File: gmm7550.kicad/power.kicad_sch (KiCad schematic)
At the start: 48 parts, among them Q1 NX6008NBK, U11 TPS3840DL28DBV, U12 ADP2164, U13 ADP2164, U3 ADP1753

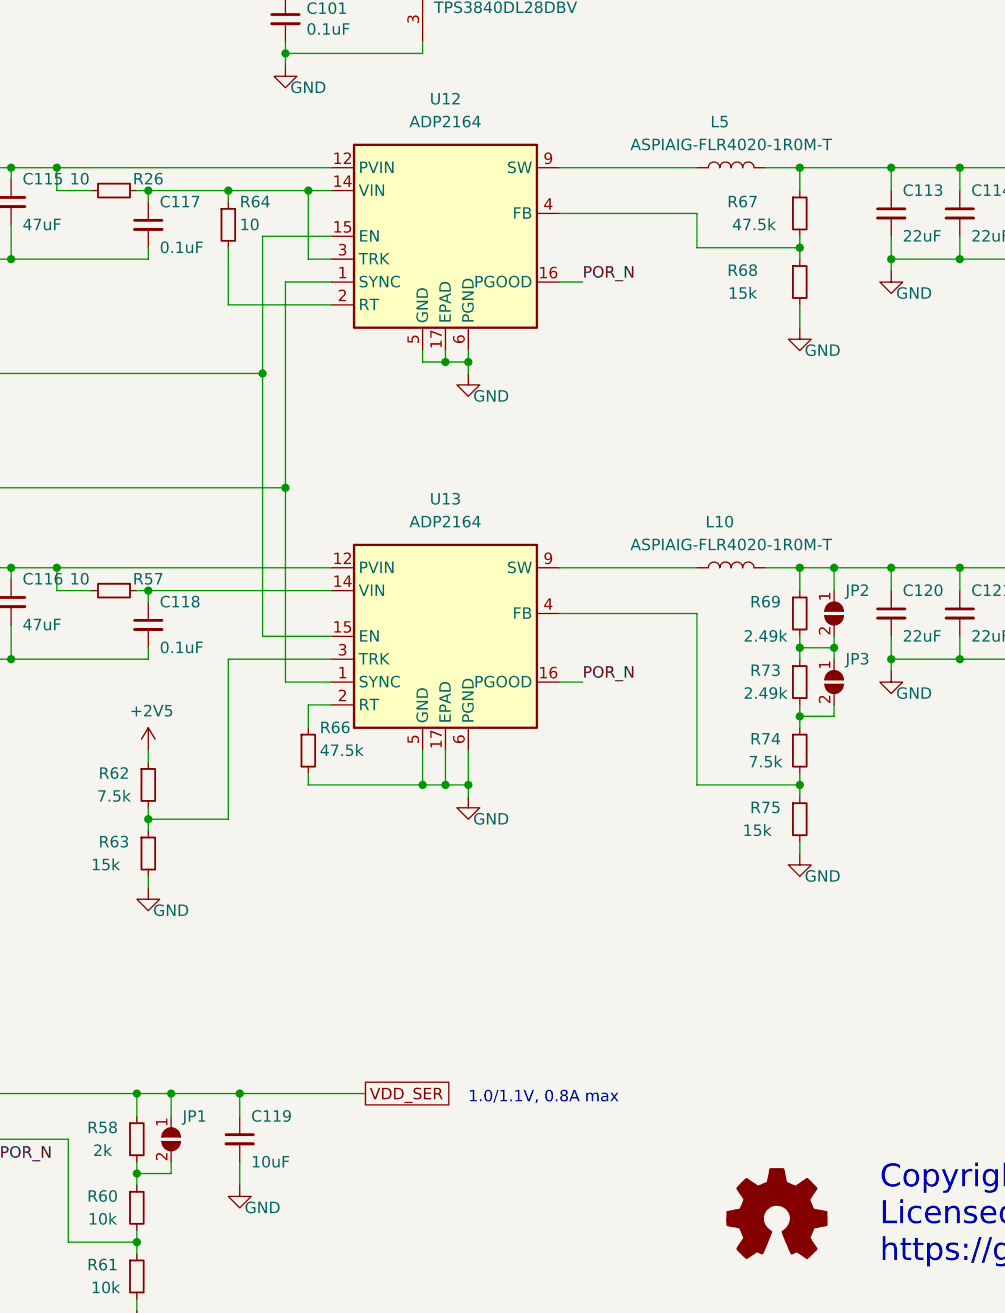
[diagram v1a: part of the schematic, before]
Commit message: Update designs to KiCad v7
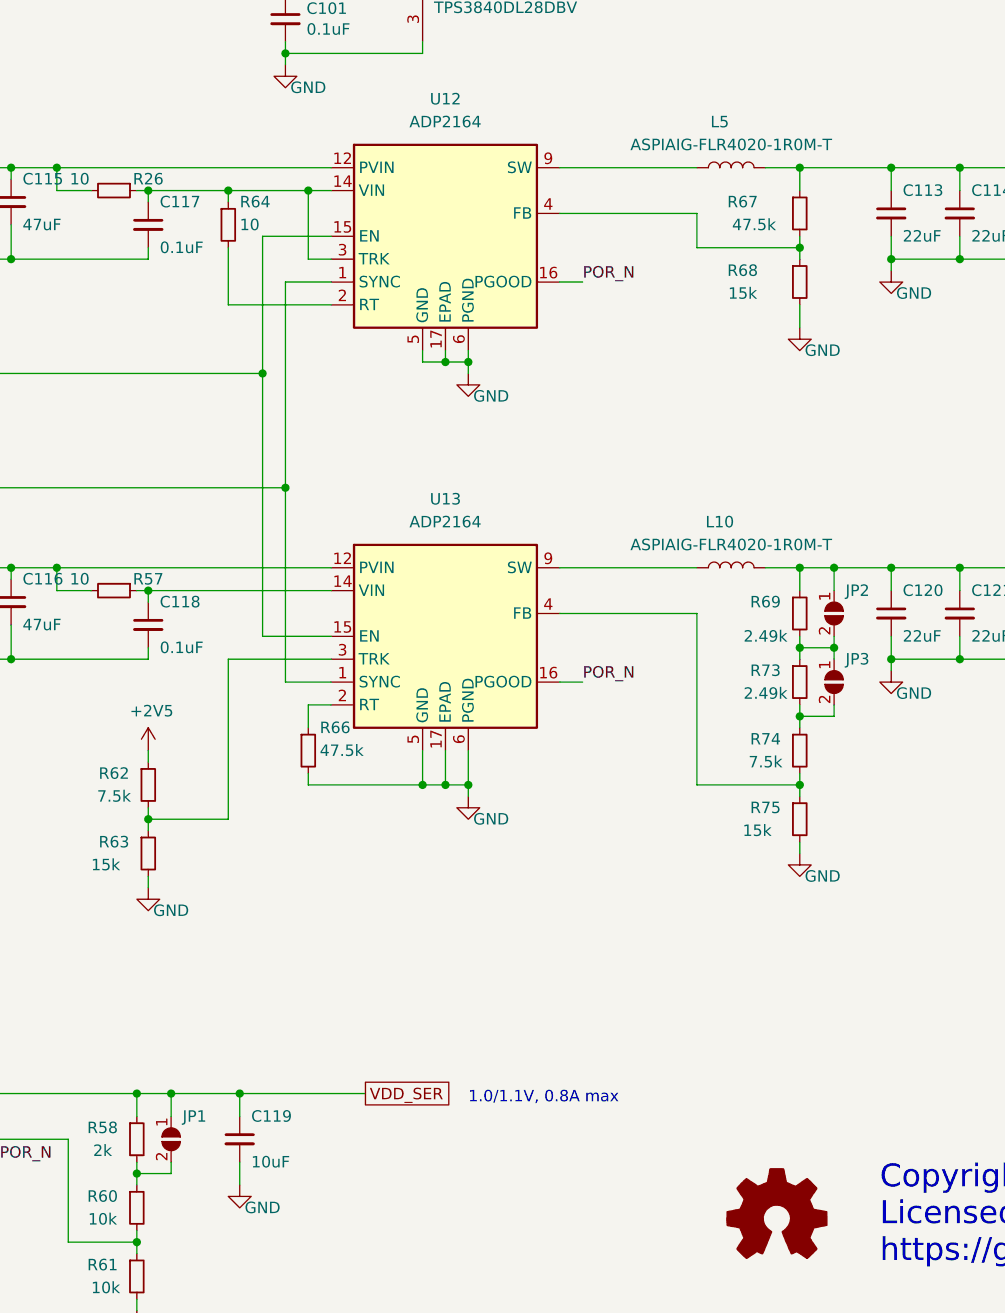
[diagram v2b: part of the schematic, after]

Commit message: Update copyright years and increment revision
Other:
- note added: "Copyright (c) 2020-2024 Anton Kuzmin Licensed under CERN-OHL-P v2 https://github.com/gmm-7550/"
- note removed: "Copyright (c) 2020-2022 Anton Kuzmin Licensed under CERN-OHL-P v2 https://github.com/ak-fau/gmm7550.git"
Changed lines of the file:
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@@
   (title_block
     (title "GateMate FPGA Module: GMM-7550")
-    (date "2022-04-24")
-    (rev "2.1")
+    (date "2022-04-27")
+    (rev "2.2")
   )
   (junction (at 129.54 80.01) (diameter 0) (color 0 0 0 0)
@@
     (effects (font (size 1.27 1.27)) (justify left bottom))
   )
-  (text "Copyright (c) 2020-2022  Anton Kuzmin\nLicensed under CERN-OHL-P v2\nhttps://github.com/ak-fau/gmm7550.git"
+  (text "Copyright (c) 2020-2024  Anton Kuzmin\nLicensed under CERN-OHL-P v2\nhttps://github.com/gmm-7550/"
     (at 198.12 179.07 0)
     (effects (font (size 2.54 2.54)) (justify left bottom))

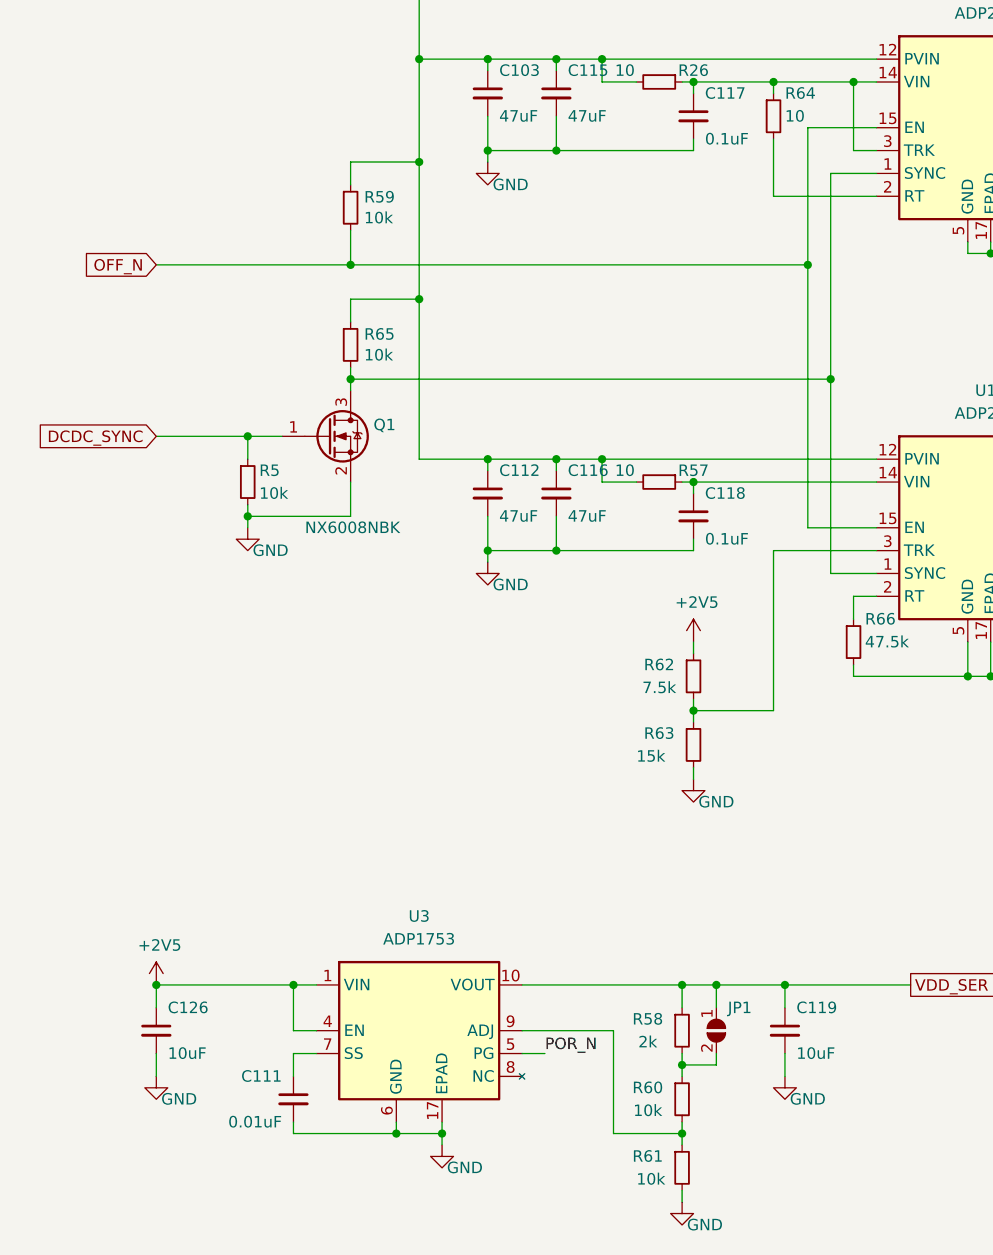
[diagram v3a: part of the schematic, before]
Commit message: Minor updates based on the test results
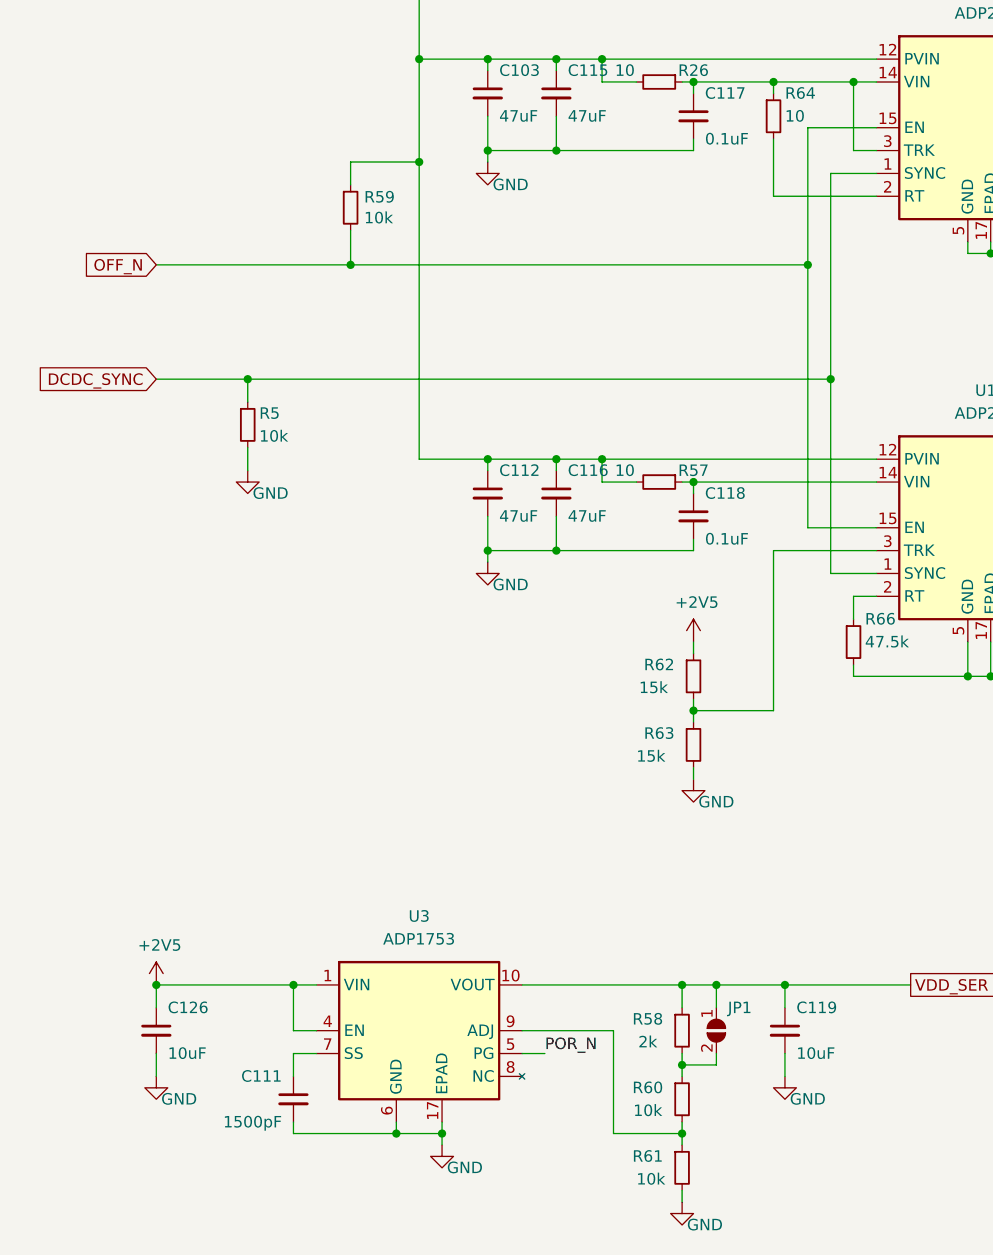
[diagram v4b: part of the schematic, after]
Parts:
- removed Q1: NX6008NBK, Package_TO_SOT_SMD:SOT-23, symbol Device:Q_NMOS_GSD
- removed R65: 10k, Resistor_SMD:R_0402_1005Metric, symbol Device:R_Small
- C111: value 0.01uF -> 1500pF
- R62: value 7.5k -> 15k
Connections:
- net DCDC_SYNC: now also U12.1 (SYNC), U13.1 (SYNC)
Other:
- moved on the sheet: R5
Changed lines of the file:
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@@
   (junction (at 93.98 111.76) (diameter 0) (color 0 0 0 0)
   )
-  (junction (at 67.31 99.06) (diameter 0) (color 0 0 0 0)
+  (junction (at 67.31 92.71) (diameter 0) (color 0 0 0 0)
   )
   (junction (at 214.63 67.31) (diameter 0) (color 0 0 0 0)
   )
-  (junction (at 67.31 107.95) (diameter 0) (color 0 0 0 0)
-  )
   (junction (at 78.74 80.01) (diameter 0) (color 0 0 0 0)
   )
@@
   (junction (at 207.01 67.31) (diameter 0) (color 0 0 0 0)
   )
-  (junction (at 78.74 92.71) (diameter 0) (color 0 0 0 0)
-  )
   (junction (at 72.39 160.02) (diameter 0) (color 0 0 0 0)
   )
@@
   (junction (at 101.6 67.31) (diameter 0) (color 0 0 0 0)
   )
-  (junction (at 86.36 83.82) (diameter 0) (color 0 0 0 0)
-  )
   (junction (at 86.36 20.32) (diameter 0) (color 0 0 0 0)
   )
@@
     (stroke (width 0) (type default))
   )
-  (wire (pts (xy 78.74 91.44) (xy 78.74 92.71))
-    (stroke (width 0) (type default))
-  )
   (wire (pts (xy 199.39 64.77) (xy 199.39 67.31))
     (stroke (width 0) (type default))
@@
     (stroke (width 0) (type default))
   )
-  (wire (pts (xy 78.74 86.36) (xy 78.74 83.82))
-    (stroke (width 0) (type default))
-  )
   (wire (pts (xy 78.74 68.58) (xy 78.74 71.12))
     (stroke (width 0) (type default))
@@
     (stroke (width 0) (type default))
   )
-  (wire (pts (xy 86.36 83.82) (xy 86.36 101.6))
-    (stroke (width 0) (type default))
-  )
   (wire (pts (xy 132.08 35.56) (xy 134.62 35.56))
     (stroke (width 0) (type default))
@@
     (stroke (width 0) (type default))
   )
-  (wire (pts (xy 78.74 83.82) (xy 86.36 83.82))
-    (stroke (width 0) (type default))
-  )
   (wire (pts (xy 93.98 107.95) (xy 93.98 111.76))
     (stroke (width 0) (type default))
@@
     (stroke (width 0) (type default))
   )
-  (wire (pts (xy 67.31 99.06) (xy 71.12 99.06))
+  (wire (pts (xy 67.31 92.71) (xy 132.08 92.71))
     (stroke (width 0) (type default))
   )
@@
     (stroke (width 0) (type default))
   )
-  (wire (pts (xy 67.31 106.68) (xy 67.31 107.95))
+  (wire (pts (xy 67.31 100.33) (xy 67.31 102.87))
     (stroke (width 0) (type default))
   )
@@
     (stroke (width 0) (type default))
   )
-  (wire (pts (xy 78.74 107.95) (xy 78.74 104.14))
-    (stroke (width 0) (type default))
-  )
   (wire (pts (xy 132.08 43.18) (xy 132.08 44.45))
     (stroke (width 0) (type default))
@@
     (stroke (width 0) (type default))
   )
-  (wire (pts (xy 78.74 92.71) (xy 78.74 93.98))
-    (stroke (width 0) (type default))
-  )
   (wire (pts (xy 177.8 125.73) (xy 189.23 125.73))
     (stroke (width 0) (type default))
@@
     (stroke (width 0) (type default))
   )
-  (wire (pts (xy 57.15 99.06) (xy 67.31 99.06))
+  (wire (pts (xy 57.15 92.71) (xy 67.31 92.71))
     (stroke (width 0) (type default))
   )
@@
     (stroke (width 0) (type default))
   )
-  (wire (pts (xy 67.31 107.95) (xy 78.74 107.95))
-    (stroke (width 0) (type default))
-  )
-  (wire (pts (xy 78.74 92.71) (xy 132.08 92.71))
-    (stroke (width 0) (type default))
-  )
   (wire (pts (xy 147.32 125.73) (xy 149.86 125.73))
     (stroke (width 0) (type default))
@@
     (stroke (width 0) (type default))
   )
-  (wire (pts (xy 67.31 107.95) (xy 67.31 109.22))
-    (stroke (width 0) (type default))
-  )
   (wire (pts (xy 189.23 132.08) (xy 189.23 133.35))
     (stroke (width 0) (type default))
   )
-  (wire (pts (xy 67.31 99.06) (xy 67.31 101.6))
+  (wire (pts (xy 67.31 92.71) (xy 67.31 95.25))
     (stroke (width 0) (type default))
   )
@@
     (stroke (width 0) (type default))
   )
-  (wire (pts (xy 86.36 68.58) (xy 86.36 83.82))
+  (wire (pts (xy 86.36 68.58) (xy 86.36 101.6))
     (stroke (width 0) (type default))
   )
@@
     )
   )
-  (global_label "DCDC_SYNC" (shape input) (at 57.15 99.06 180) (fields_autoplaced)
+  (global_label "DCDC_SYNC" (shape input) (at 57.15 92.71 180) (fields_autoplaced)
     (effects (font (size 1.27 1.27)) (justify right))
-    (property "Intersheetrefs" "${INTERSHEET_REFS}" (at 43.6002 98.9806 0)
+    (property "Intersheetrefs" "${INTERSHEET_REFS}" (at 43.6002 92.6306 0)
       (effects (font (size 1.27 1.27)) (justify right) hide)
     )
@@
     )
   )
-  (symbol (lib_id "Device:R_Small") (at 78.74 88.9 0) (unit 1)
-    (in_bom yes) (on_board yes) (dnp no)
-    (property "Reference" "R65" (at 80.2386 87.7316 0)
-      (effects (font (size 1.27 1.27)) (justify left))
-    )
-    (property "Value" "10k" (at 80.2386 90.043 0)
-      (effects (font (size 1.27 1.27)) (justify left))
-    )
-    (property "Footprint" "Resistor_SMD:R_0402_1005Metric" (at 78.74 88.9 0)
-      (effects (font (size 1.27 1.27)) hide)
-    )
-    (property "Datasheet" "~" (at 78.74 88.9 0)
-      (effects (font (size 1.27 1.27)) hide)
-    )
-    (pin "1")
-    (pin "2")
-    (instances
-      (project "gmm"
-        (path "/eec0112f-83d8-4749-a00d-7d0cfc1ef163/00000000-0000-0000-0000-00005e928e3d"
-          (reference "R65") (unit 1)
-        )
-      )
-    )
-  )
   (symbol (lib_id "power:GND") (at 199.39 68.58 0) (unit 1)
     (in_bom yes) (on_board yes) (dnp no)
@@
     )
   )
-  (symbol (lib_id "Device:Q_NMOS_GSD") (at 76.2 99.06 0) (unit 1)
-    (in_bom yes) (on_board yes) (dnp no)
-    (property "Reference" "Q1" (at 81.28 97.79 0)
-      (effects (font (size 1.27 1.27)) (justify left))
-    )
-    (property "Value" "NX6008NBK" (at 73.66 109.22 0)
-      (effects (font (size 1.27 1.27)) (justify left))
-    )
-    (property "Footprint" "Package_TO_SOT_SMD:SOT-23" (at 81.28 96.52 0)
-      (effects (font (size 1.27 1.27)) hide)
-    )
-    (property "Datasheet" "~" (at 76.2 99.06 0)
-      (effects (font (size 1.27 1.27)) hide)
-    )
-    (pin "1")
-    (pin "2")
-    (pin "3")
-    (instances
-      (project "gmm"
-        (path "/eec0112f-83d8-4749-a00d-7d0cfc1ef163/00000000-0000-0000-0000-00005e928e3d"
-          (reference "Q1") (unit 1)
-        )
-      )
-    )
-  )
   (symbol (lib_id "Device:R_Small") (at 115.57 172.72 0) (unit 1)
     (in_bom yes) (on_board yes) (dnp no)
@@
     )
   )
-  (symbol (lib_id "Device:R_Small") (at 67.31 104.14 0) (unit 1)
-    (in_bom yes) (on_board yes) (dnp no)
-    (property "Reference" "R5" (at 68.58 102.87 0)
-      (effects (font (size 1.27 1.27)) (justify left))
-    )
-    (property "Value" "10k" (at 68.58 105.41 0)
-      (effects (font (size 1.27 1.27)) (justify left))
-    )
-    (property "Footprint" "Resistor_SMD:R_0402_1005Metric" (at 67.31 104.14 0)
-      (effects (font (size 1.27 1.27)) hide)
-    )
-    (property "Datasheet" "~" (at 67.31 104.14 0)
+  (symbol (lib_id "Device:R_Small") (at 67.31 97.79 0) (unit 1)
+    (in_bom yes) (on_board yes) (dnp no)
+    (property "Reference" "R5" (at 68.58 96.52 0)
+      (effects (font (size 1.27 1.27)) (justify left))
+    )
+    (property "Value" "10k" (at 68.58 99.06 0)
+      (effects (font (size 1.27 1.27)) (justify left))
+    )
+    (property "Footprint" "Resistor_SMD:R_0402_1005Metric" (at 67.31 97.79 0)
+      (effects (font (size 1.27 1.27)) hide)
+    )
+    (property "Datasheet" "~" (at 67.31 97.79 0)
       (effects (font (size 1.27 1.27)) hide)
     )
@@
     )
   )
-  (symbol (lib_id "power:GND") (at 67.31 109.22 0) (unit 1)
-    (in_bom yes) (on_board yes) (dnp no)
-    (property "Reference" "#PWR0164" (at 67.31 115.57 0)
-      (effects (font (size 1.27 1.27)) hide)
-    )
-    (property "Value" "GND" (at 69.85 111.76 0)
-      (effects (font (size 1.27 1.27)))
-    )
-    (property "Footprint" "" (at 67.31 109.22 0)
-      (effects (font (size 1.27 1.27)) hide)
-    )
-    (property "Datasheet" "" (at 67.31 109.22 0)
+  (symbol (lib_id "power:GND") (at 67.31 102.87 0) (unit 1)
+    (in_bom yes) (on_board yes) (dnp no)
+    (property "Reference" "#PWR0164" (at 67.31 109.22 0)
+      (effects (font (size 1.27 1.27)) hide)
+    )
+    (property "Value" "GND" (at 69.85 105.41 0)
+      (effects (font (size 1.27 1.27)))
+    )
+    (property "Footprint" "" (at 67.31 102.87 0)
+      (effects (font (size 1.27 1.27)) hide)
+    )
+    (property "Datasheet" "" (at 67.31 102.87 0)
       (effects (font (size 1.27 1.27)) hide)
     )
@@
       (effects (font (size 1.27 1.27)))
     )
-    (property "Value" "7.5k" (at 113.03 127 0)
+    (property "Value" "15k" (at 112.395 127 0)
       (effects (font (size 1.27 1.27)))
     )
@@
       (effects (font (size 1.27 1.27)) (justify left))
     )
-    (property "Value" "0.01uF" (at 71.12 175.26 0)
-      (effects (font (size 1.27 1.27)) (justify left))
-    )
+    (property "Value" "1500pF" (at 71.12 175.26 0)
+      (effects (font (size 1.27 1.27)) (justify left))
+    )
